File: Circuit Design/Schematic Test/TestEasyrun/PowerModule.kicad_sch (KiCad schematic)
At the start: 0 parts

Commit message: Power integration
Power integration
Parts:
- added CB_5v0: 0.47u, symbol Device:C
- added C_Buck3v3, C_Buck5v0, C_DTCS_3v3, C_DTCS_5v0: 1u, symbol Device:C
- added C_CT_PWM_3v3, C_CT_PWM_5v0: 1n, symbol Device:C
- added C_rec: 100u, symbol Device:C
- added DB_5v0: 1N47xxA, Diode_THT:D_DO-41_SOD81_P10.16mm_Horizontal, symbol Diode:1N47xxA
- added D_Buck3v3, D_Buck5v0, D_S1, D_S2: 1N5822, Diode_THT:D_DO-201AD_P15.24mm_Horizontal, symbol Diode:1N5822
- added L_Buck3v3, L_Buck5v0: 20u, symbol Device:L
- added Q_3v3, Q_5v0: Q_NMOS_DGS, symbol Device:Q_NMOS_DGS
- added R_DTCS_3v3, R_DTCS_5v0: 680, symbol Device:R
- added R_DTC_3v3, R_DTC_5v0: 1k, symbol Device:R
- added R_RT_PWM_3v3, R_RT_PWM_5v0: 6.8k, symbol Device:R
- added U_Driver5v0: IR2110, Package_DIP:DIP-14_W7.62mm, symbol Driver_FET:IR2110
- added U_PWM_3v3, U_PWM_5v0: TL494CDR, SOIC127P600X175-16N, symbol TL494CDR:TL494CDR
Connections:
- new net: C_DTCS_5v0.1, R_DTCS_5v0.1
- new net: C_DTCS_5v0.2, R_DTC_5v0.1, U_PWM_5v0.4 (DTC)
- new net: C_DTCS_3v3.1, R_DTCS_3v3.1
- new net: C_DTCS_3v3.2, R_DTC_3v3.1, U_PWM_3v3.4 (DTC)
- new net: C_CT_PWM_5v0.1, U_PWM_5v0.5 (CT)
- new net: D_Buck3v3.1 (K), L_Buck3v3.1, Q_3v3.3 (S)
- new net: CB_5v0.1, DB_5v0.1 (K), U_Driver5v0.6 (VB)
- new net: R_RT_PWM_5v0.1, U_PWM_5v0.6 (RT)
- new net: C_CT_PWM_3v3.1, U_PWM_3v3.5 (CT)
- new net: R_RT_PWM_3v3.1, U_PWM_3v3.6 (RT)
- new net 3v3: C_Buck3v3.1, L_Buck3v3.2, U_PWM_3v3.1 (1IN+), U_PWM_3v3.16 (2IN+)
- new net 5v0: C_Buck5v0.1, L_Buck5v0.2, U_PWM_5v0.1 (1IN+), U_PWM_5v0.16 (2IN+)
- new net GND: C_Buck3v3.2, C_Buck5v0.2, C_CT_PWM_3v3.2, C_CT_PWM_5v0.2, C_rec.2, D_Buck3v3.2 (A), D_Buck5v0.2 (A), R_DTC_3v3.2, R_DTC_5v0.2, R_RT_PWM_3v3.2, R_RT_PWM_5v0.2, U_Driver5v0.11 (SD), U_Driver5v0.12 (LIN), U_Driver5v0.13 (VSS), U_Driver5v0.2 (COM), U_PWM_3v3.13 (OUTPUT_CTRL), U_PWM_3v3.7 (GND), U_PWM_5v0.13 (OUTPUT_CTRL), U_PWM_5v0.7 (GND)
- new net H_PWM_5v0: Q_5v0.2 (G), U_Driver5v0.7 (HO)
- new net PWM_3v3: U_PWM_3v3.10 (E2), U_PWM_3v3.9 (E1)
- new net PWM_5v0: U_Driver5v0.10 (HIN), U_PWM_5v0.10 (E2), U_PWM_5v0.9 (E1)
- new net Ref_3v3: R_DTCS_3v3.2, U_PWM_3v3.14 (REF), U_PWM_3v3.15 (2IN−), U_PWM_3v3.2 (1IN−)
- new net Ref_5v0: DB_5v0.2 (A), R_DTCS_5v0.2, U_Driver5v0.3 (VCC), U_Driver5v0.9 (VDD), U_PWM_5v0.14 (REF), U_PWM_5v0.15 (2IN−), U_PWM_5v0.2 (1IN−)
- new net Tab_2: D_S2.2 (A)
- new net Tap_1: D_S1.2 (A)
- new net VS_5v0: CB_5v0.2, D_Buck5v0.1 (K), L_Buck5v0.1, Q_5v0.3 (S), U_Driver5v0.5 (VS)
- new net Vo_rec: C_rec.1, D_S1.1 (K), D_S2.1 (K), Q_3v3.1 (D), Q_5v0.1 (D), U_PWM_3v3.11 (C2), U_PWM_3v3.12 (VCC), U_PWM_3v3.8 (C1), U_PWM_5v0.11 (C2), U_PWM_5v0.12 (VCC), U_PWM_5v0.8 (C1)
- no-connect marks 0 -> 3

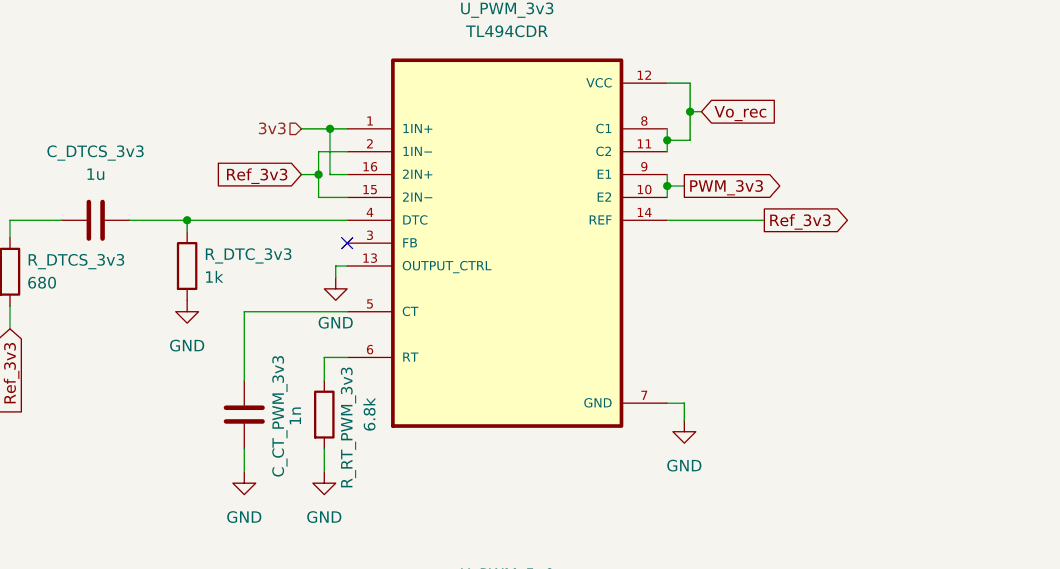
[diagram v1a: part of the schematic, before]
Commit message: 3v3 Controller fixed
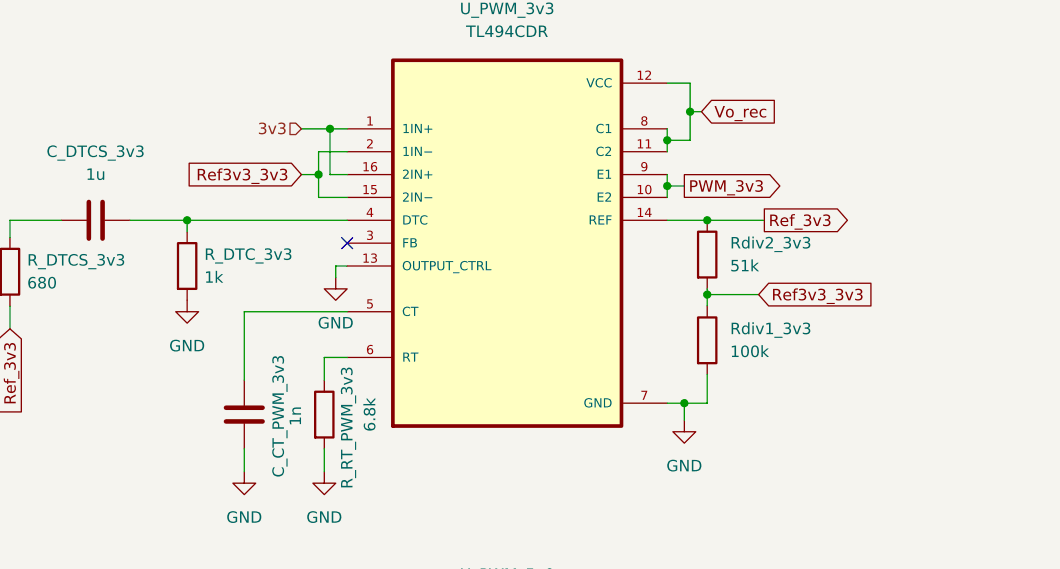
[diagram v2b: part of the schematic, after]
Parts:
- added Rdiv1_3v3: 100k, symbol Device:R
- added Rdiv2_3v3: 51k, symbol Device:R
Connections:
- net GND: now also Rdiv1_3v3.2
- net Ref_3v3: now also Rdiv2_3v3.1; no longer U_PWM_3v3.15 (2IN−), U_PWM_3v3.2 (1IN−)
- new net Ref3v3_3v3: Rdiv1_3v3.1, Rdiv2_3v3.2, U_PWM_3v3.15 (2IN−), U_PWM_3v3.2 (1IN−)
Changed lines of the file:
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@@
   (junction (at 71.755 74.295) (diameter 0) (color 0 0 0 0)
   )
+  (junction (at 127 94.615) (diameter 0) (color 0 0 0 0)
+  )
   (junction (at 254 114.3) (diameter 0) (color 0 0 0 0)
   )
@@
   (junction (at 127.635 125.095) (diameter 0) (color 0 0 0 0)
   )
+  (junction (at 129.54 74.295) (diameter 0) (color 0 0 0 0)
+  )
   (junction (at 232.41 114.3) (diameter 0) (color 0 0 0 0)
   )
@@
   )
   (junction (at 87.63 64.135) (diameter 0) (color 0 0 0 0)
+  )
+  (junction (at 129.54 82.55) (diameter 0) (color 0 0 0 0)
   )
   (junction (at 125.095 128.27) (diameter 0) (color 0 0 0 0)
@@
     (stroke (width 0) (type default) (color 0 0 0 0))
   )
+  (wire (pts (xy 129.54 74.295) (xy 135.89 74.295))
+    (stroke (width 0) (type default) (color 0 0 0 0))
+  )
   (wire (pts (xy 52.07 76.2) (xy 52.07 74.295))
     (stroke (width 0) (type default) (color 0 0 0 0))
@@
     (stroke (width 0) (type default) (color 0 0 0 0))
   )
+  (wire (pts (xy 129.54 82.55) (xy 129.54 83.82))
+    (stroke (width 0) (type default) (color 0 0 0 0))
+  )
   (wire (pts (xy 71.755 74.295) (xy 71.755 75.565))
     (stroke (width 0) (type default) (color 0 0 0 0))
@@
     (stroke (width 0) (type default) (color 0 0 0 0))
   )
+  (wire (pts (xy 129.54 91.44) (xy 129.54 94.615))
+    (stroke (width 0) (type default) (color 0 0 0 0))
+  )
   (wire (pts (xy 125.095 121.92) (xy 127.635 121.92))
     (stroke (width 0) (type default) (color 0 0 0 0))
@@
     (stroke (width 0) (type default) (color 0 0 0 0))
   )
+  (wire (pts (xy 129.54 82.55) (xy 135.255 82.55))
+    (stroke (width 0) (type default) (color 0 0 0 0))
+  )
   (wire (pts (xy 193.675 146.685) (xy 193.675 151.765))
     (stroke (width 0) (type default) (color 0 0 0 0))
@@
     (stroke (width 0) (type default) (color 0 0 0 0))
   )
+  (wire (pts (xy 127 94.615) (xy 129.54 94.615))
+    (stroke (width 0) (type default) (color 0 0 0 0))
+  )
   (wire (pts (xy 89.535 66.675) (xy 86.36 66.675))
     (stroke (width 0) (type default) (color 0 0 0 0))
@@
     (stroke (width 0) (type default) (color 0 0 0 0))
   )
-  (wire (pts (xy 125.095 74.295) (xy 135.89 74.295))
+  (wire (pts (xy 125.095 74.295) (xy 129.54 74.295))
     (stroke (width 0) (type default) (color 0 0 0 0))
   )
@@
   )
   (wire (pts (xy 87.63 132.08) (xy 89.535 132.08))
+    (stroke (width 0) (type default) (color 0 0 0 0))
+  )
+  (wire (pts (xy 129.54 81.915) (xy 129.54 82.55))
     (stroke (width 0) (type default) (color 0 0 0 0))
   )
@@
     )
   )
-  (global_label "Ref_3v3" (shape input) (at 84.455 69.215 180) (fields_autoplaced)
+  (global_label "Ref3v3_3v3" (shape input) (at 84.455 69.215 180) (fields_autoplaced)
     (effects (font (size 1.27 1.27)) (justify right))
-    (property "Intersheet References" "${INTERSHEET_REFS}" (id 0) (at 74.6033 69.1356 0)
+    (property "Intersheet References" "${INTERSHEET_REFS}" (id 0) (at 71.2167 69.1356 0)
       (effects (font (size 1.27 1.27)) (justify right) hide)
     )
@@
     )
   )
+  (global_label "Ref3v3_3v3" (shape input) (at 135.255 82.55 0) (fields_autoplaced)
+    (effects (font (size 1.27 1.27)) (justify left))
+    (property "Intersheet References" "${INTERSHEET_REFS}" (id 0) (at 148.4933 82.4706 0)
+      (effects (font (size 1.27 1.27)) (justify left) hide)
+    )
+  )
   (global_label "Ref_5v0" (shape input) (at 195.58 151.765 0) (fields_autoplaced)
     (effects (font (size 1.27 1.27)) (justify left))
@@
     )
     (property "Datasheet" "~" (id 3) (at 78.105 158.75 0)
+      (effects (font (size 1.27 1.27)) hide)
+    )
+    (pin "1")
+    (pin "2")
+  )
+  (symbol (lib_id "Device:R") (at 129.54 87.63 0) (unit 1)
+    (in_bom yes) (on_board yes) (fields_autoplaced)
+    (property "Reference" "Rdiv1_3v3" (id 0) (at 132.08 86.3599 0)
+      (effects (font (size 1.27 1.27)) (justify left))
+    )
+    (property "Value" "100k" (id 1) (at 132.08 88.8999 0)
+      (effects (font (size 1.27 1.27)) (justify left))
+    )
+    (property "Footprint" "" (id 2) (at 127.762 87.63 90)
+      (effects (font (size 1.27 1.27)) hide)
+    )
+    (property "Datasheet" "~" (id 3) (at 129.54 87.63 0)
       (effects (font (size 1.27 1.27)) hide)
     )
@@
       (effects (font (size 1.27 1.27)) hide)
     )
+    (pin "1")
+    (pin "2")
+  )
+  (symbol (lib_id "Device:R") (at 129.54 78.105 0) (unit 1)
+    (in_bom yes) (on_board yes) (fields_autoplaced)
+    (property "Reference" "Rdiv2_3v3" (id 0) (at 132.08 76.8349 0)
+      (effects (font (size 1.27 1.27)) (justify left))
+    )
+    (property "Value" "51k" (id 1) (at 132.08 79.3749 0)
+      (effects (font (size 1.27 1.27)) (justify left))
+    )
+    (property "Footprint" "" (id 2) (at 127.762 78.105 90)
+      (effects (font (size 1.27 1.27)) hide)
+    )
+    (property "Datasheet" "~" (id 3) (at 129.54 78.105 0)
+      (effects (font (size 1.27 1.27)) hide)
+    )

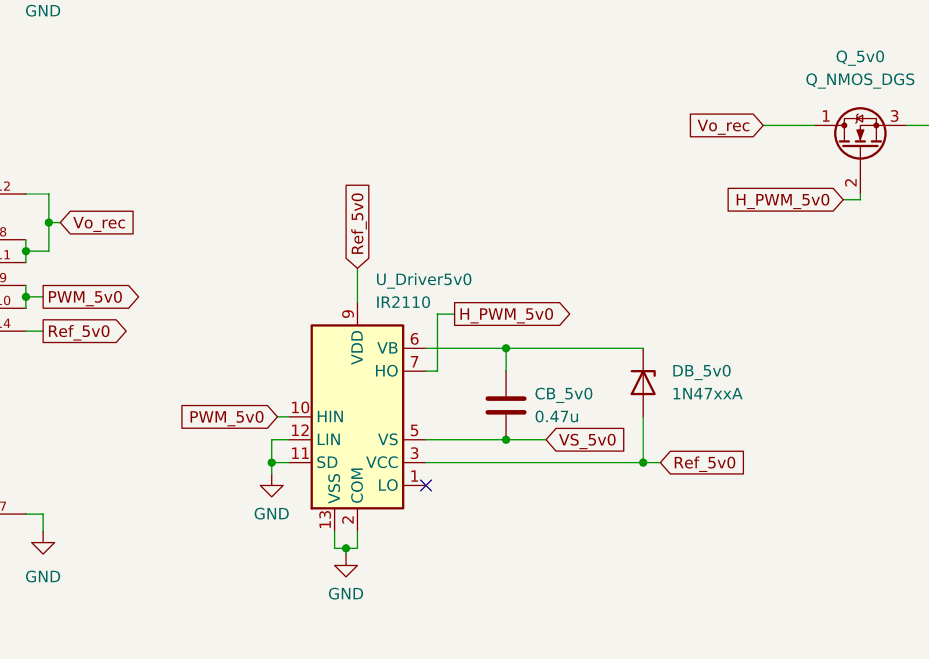
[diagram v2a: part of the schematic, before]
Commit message: Old gate driver removed, looking for something else
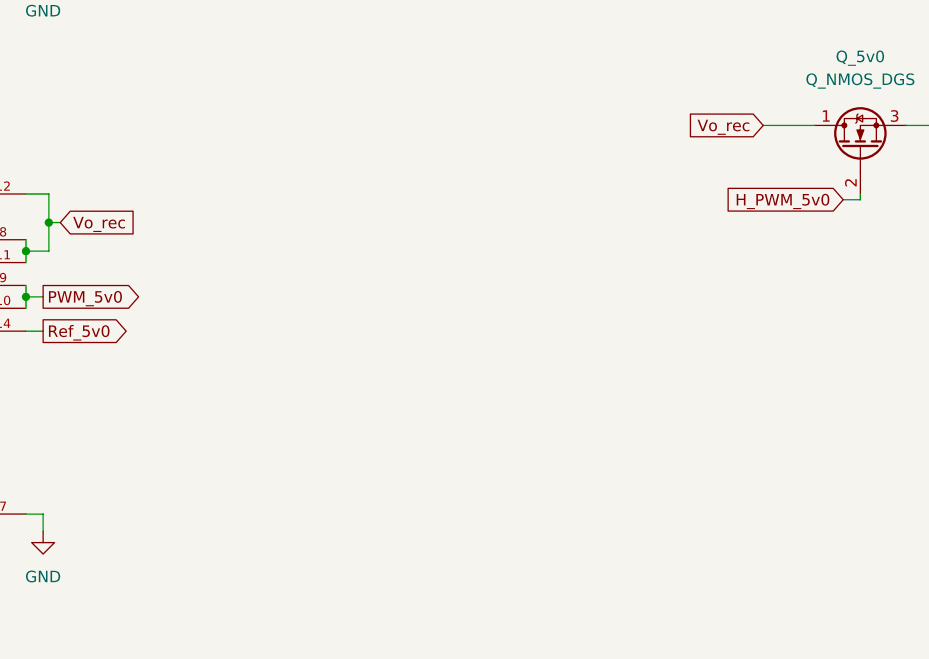
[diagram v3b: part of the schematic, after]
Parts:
- removed CB_5v0: 0.47u, symbol Device:C
- removed DB_5v0: 1N47xxA, Diode_THT:D_DO-41_SOD81_P10.16mm_Horizontal, symbol Diode:1N47xxA
- removed U_Driver5v0: IR2110, Package_DIP:DIP-14_W7.62mm, symbol Driver_FET:IR2110
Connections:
- no-connect marks 3 -> 2

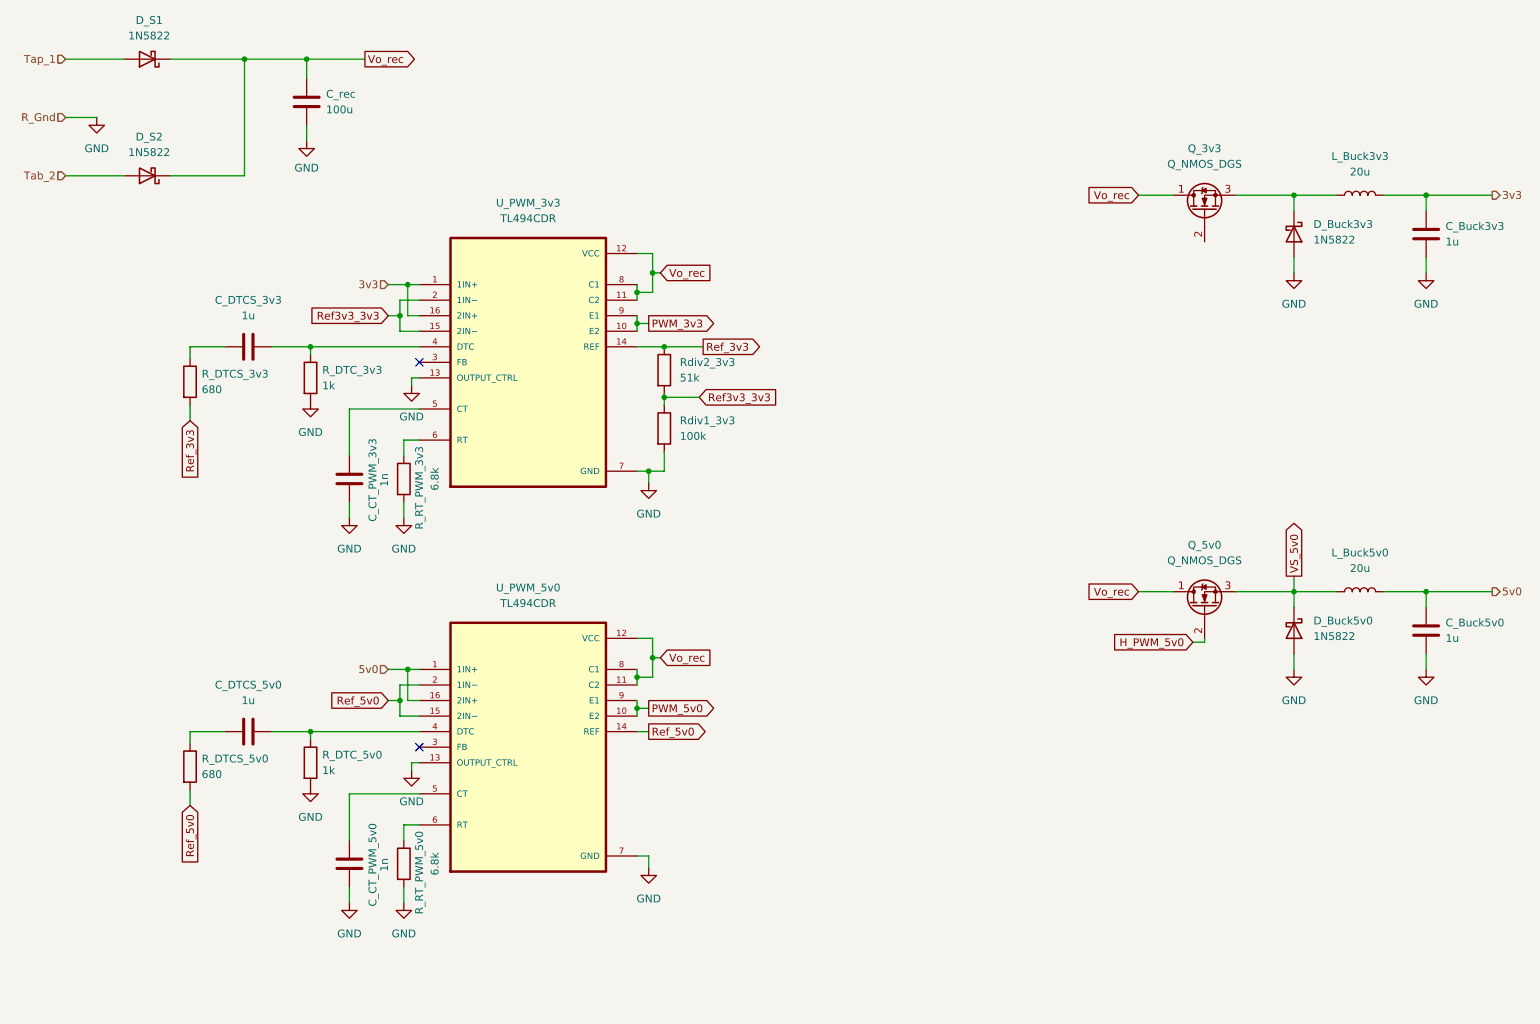
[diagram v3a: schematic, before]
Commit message: Footprints added and new drivers designed
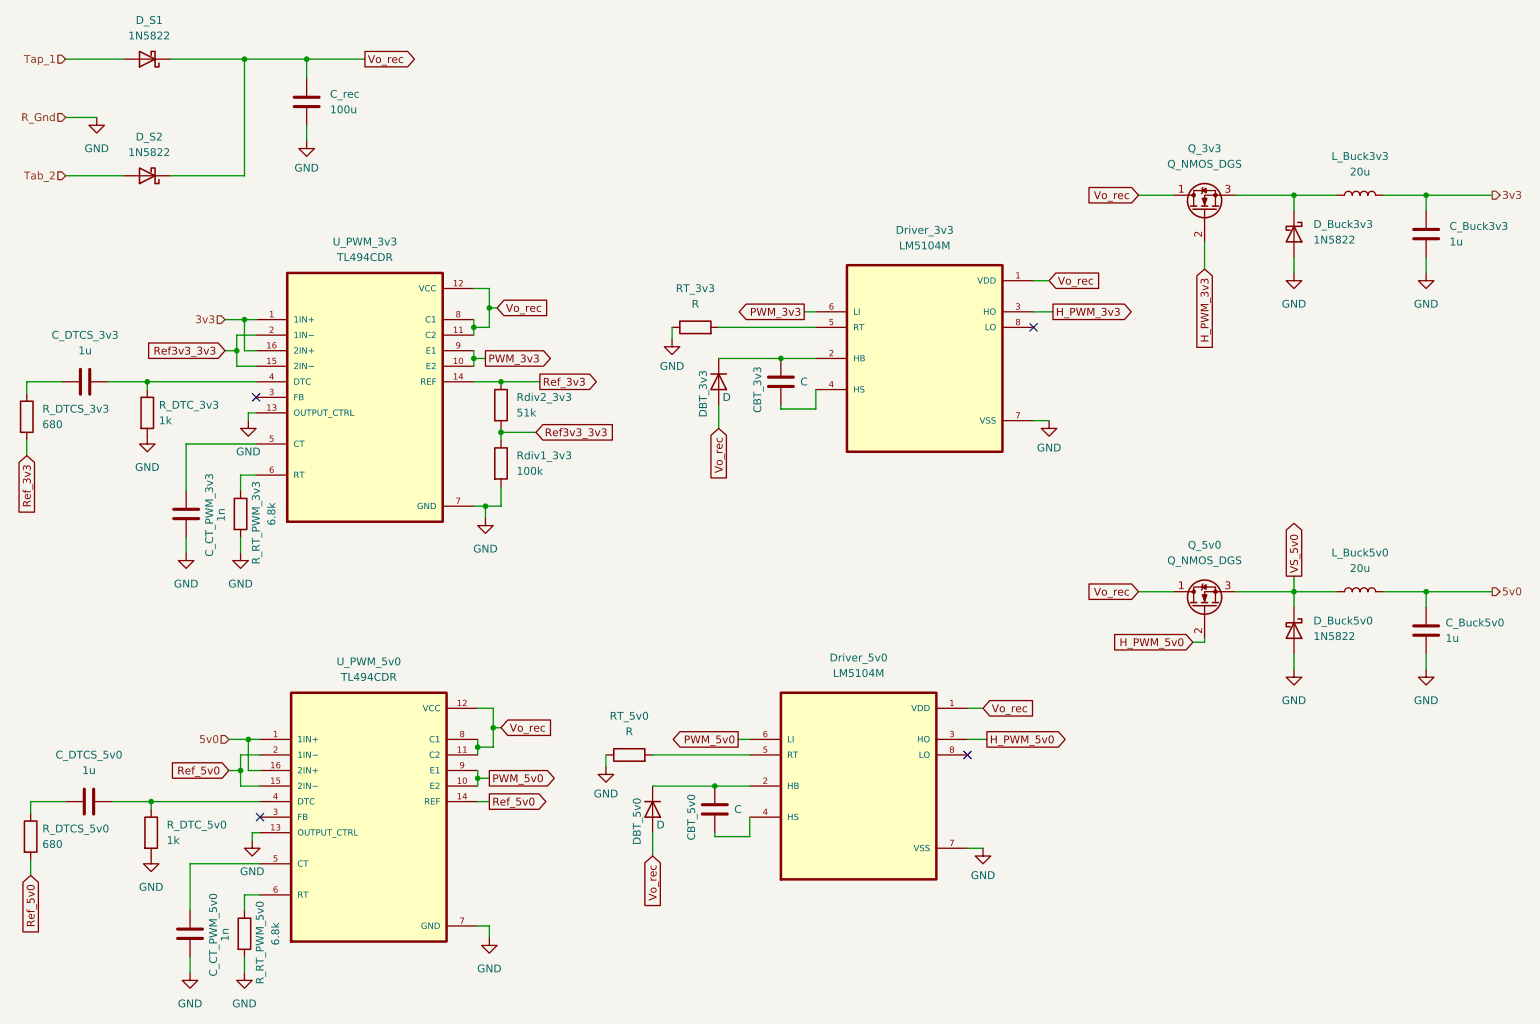
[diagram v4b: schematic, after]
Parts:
- added CBT_3v3, CBT_5v0: C, Capacitor_SMD:C_0805_2012Metric_Pad1.18x1.45mm_HandSolder, symbol Device:C
- added DBT_3v3, DBT_5v0: D, Diode_THT:D_DO-201AD_P15.24mm_Horizontal, symbol Device:D
- added Driver_3v3, Driver_5v0: LM5104M, LM5104M:SOIC127P599X175-8N, symbol LM5104M:LM5104M
- added RT_3v3, RT_5v0: R, Resistor_SMD:R_0805_2012Metric_Pad1.20x1.40mm_HandSolder, symbol Device:R
- C_Buck3v3, C_Buck5v0: footprint (none) -> Capacitor_SMD:CP_Elec_6.3x5.8
- C_CT_PWM_3v3, C_CT_PWM_5v0, C_DTCS_3v3, C_DTCS_5v0, C_rec: footprint (none) -> Capacitor_SMD:C_0805_2012Metric_Pad1.18x1.45mm_HandSolder
- R_DTCS_3v3, R_DTCS_5v0, R_DTC_3v3, R_DTC_5v0, R_RT_PWM_3v3, R_RT_PWM_5v0, Rdiv1_3v3, Rdiv2_3v3: footprint (none) -> Resistor_SMD:R_0805_2012Metric_Pad1.20x1.40mm_HandSolder
- U_PWM_3v3, U_PWM_5v0: footprint SOIC127P600X175-16N -> TL494CDR_PWM:SOIC127P600X175-16N
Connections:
- net GND: now also Driver_3v3.7 (VSS), Driver_5v0.7 (VSS), RT_3v3.1, RT_5v0.1
- net H_PWM_5v0: now also Driver_5v0.3 (HO)
- net PWM_3v3: now also Driver_3v3.6 (LI)
- net PWM_5v0: now also Driver_5v0.6 (LI)
- net Vo_rec: now also DBT_3v3.2 (A), DBT_5v0.2 (A), Driver_3v3.1 (VDD), Driver_5v0.1 (VDD)
- net H_PWM_3v3: now reaches Q_3v3.2 (G)
- net H_PWM_3v3: now also Driver_3v3.3 (HO)
- new net: CBT_3v3.1, DBT_3v3.1 (K), Driver_3v3.2 (HB)
- new net: CBT_5v0.1, DBT_5v0.1 (K), Driver_5v0.2 (HB)
- new net: CBT_5v0.2, Driver_5v0.4 (HS)
- new net: CBT_3v3.2, Driver_3v3.4 (HS)
- new net: Driver_5v0.5 (RT), RT_5v0.2
- new net: Driver_3v3.5 (RT), RT_3v3.2
- no-connect marks 2 -> 4
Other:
- moved on the sheet: C_CT_PWM_3v3, C_CT_PWM_5v0, C_DTCS_3v3, C_DTCS_5v0, R_DTCS_3v3, R_DTCS_5v0, R_DTC_3v3, R_DTC_5v0, R_RT_PWM_3v3, R_RT_PWM_5v0, Rdiv1_3v3, Rdiv2_3v3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
